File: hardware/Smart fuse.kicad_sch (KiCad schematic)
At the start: 2 parts, among them U14 SMART FUSE

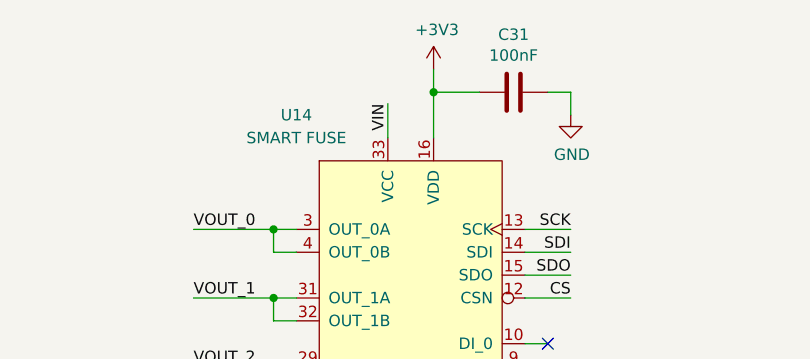
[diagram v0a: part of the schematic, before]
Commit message: changed clock and 5v converter coils, footprints rearrange commponets to fit the need now the board connector is vertical not horizontal relative to the pcb's longest side
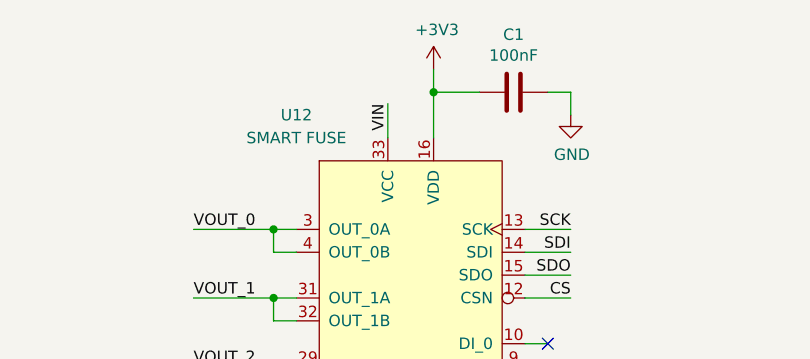
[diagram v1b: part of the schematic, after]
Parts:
- renumbered C31 to C1, U14 to U12
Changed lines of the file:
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@@
   (symbol (lib_id "power:GND") (at 144.78 137.16 0)
     (in_bom yes) (on_board yes)
-    (property "Reference" "#PWR069" (id 0) (at 144.78 143.51 0)
+    (property "Reference" "#PWR063" (id 0) (at 144.78 143.51 0)
       (effects (font (size 1.27 1.27)) hide)
     )
@@
   (symbol (lib_id "Device:C") (at 156.21 68.58 270)
     (in_bom yes) (on_board yes)
-    (property "Reference" "C31" (id 0) (at 156.21 62.1792 90))
+    (property "Reference" "C1" (id 0) (at 156.21 62.1792 90))
     (property "Value" "100nF" (id 1) (at 156.21 64.4906 90))
     (property "Footprint" "Capacitor_SMD:C_0603_1608Metric" (id 2) (at 152.4 69.5452 0)
@@
   (symbol (lib_id "power:GND") (at 162.56 71.12 0)
     (in_bom yes) (on_board yes)
-    (property "Reference" "#PWR071" (id 0) (at 162.56 77.47 0)
+    (property "Reference" "#PWR065" (id 0) (at 162.56 77.47 0)
       (effects (font (size 1.27 1.27)) hide)
     )
@@
   (symbol (lib_id "VN9D30Q100F:VN9D30Q100F") (at 144.78 76.2 0)
     (in_bom yes) (on_board yes)
-    (property "Reference" "U14" (id 0) (at 132.08 71.12 0))
+    (property "Reference" "U12" (id 0) (at 132.08 71.12 0))
     (property "Value" "SMART FUSE" (id 1) (at 132.08 73.66 0))
     (property "Footprint" "VN9D30Q100F:QFN-32_EP_6x6_Pitch0.5mm" (id 2) (at 154.94 72.39 0)
@@
   (symbol (lib_id "power:+3V3") (at 147.32 66.04 0)
     (in_bom yes) (on_board yes)
-    (property "Reference" "#PWR070" (id 0) (at 147.32 69.85 0)
+    (property "Reference" "#PWR064" (id 0) (at 147.32 69.85 0)
       (effects (font (size 1.27 1.27)) hide)
     )

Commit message: minor improvements
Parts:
- renumbered C1 to C32, U12 to U15
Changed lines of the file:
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@@
   (symbol (lib_id "power:GND") (at 144.78 137.16 0)
     (in_bom yes) (on_board yes)
-    (property "Reference" "#PWR063" (id 0) (at 144.78 143.51 0)
+    (property "Reference" "#PWR072" (id 0) (at 144.78 143.51 0)
       (effects (font (size 1.27 1.27)) hide)
     )
@@
   (symbol (lib_id "Device:C") (at 156.21 68.58 270)
     (in_bom yes) (on_board yes)
-    (property "Reference" "C1" (id 0) (at 156.21 62.1792 90))
+    (property "Reference" "C32" (id 0) (at 156.21 62.1792 90))
     (property "Value" "100nF" (id 1) (at 156.21 64.4906 90))
     (property "Footprint" "Capacitor_SMD:C_0603_1608Metric" (id 2) (at 152.4 69.5452 0)
@@
   (symbol (lib_id "power:GND") (at 162.56 71.12 0)
     (in_bom yes) (on_board yes)
-    (property "Reference" "#PWR065" (id 0) (at 162.56 77.47 0)
+    (property "Reference" "#PWR074" (id 0) (at 162.56 77.47 0)
       (effects (font (size 1.27 1.27)) hide)
     )
@@
   (symbol (lib_id "VN9D30Q100F:VN9D30Q100F") (at 144.78 76.2 0)
     (in_bom yes) (on_board yes)
-    (property "Reference" "U12" (id 0) (at 132.08 71.12 0))
+    (property "Reference" "U15" (id 0) (at 132.08 71.12 0))
     (property "Value" "SMART FUSE" (id 1) (at 132.08 73.66 0))
     (property "Footprint" "VN9D30Q100F:QFN-32_EP_6x6_Pitch0.5mm" (id 2) (at 154.94 72.39 0)
@@
   (symbol (lib_id "power:+3V3") (at 147.32 66.04 0)
     (in_bom yes) (on_board yes)
-    (property "Reference" "#PWR064" (id 0) (at 147.32 69.85 0)
+    (property "Reference" "#PWR073" (id 0) (at 147.32 69.85 0)
       (effects (font (size 1.27 1.27)) hide)
     )

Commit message: preproduction bug fixes
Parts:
- renumbered C32 to C1, U15 to U12
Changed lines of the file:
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@@
   (symbol (lib_id "power:GND") (at 144.78 137.16 0)
     (in_bom yes) (on_board yes)
-    (property "Reference" "#PWR072" (id 0) (at 144.78 143.51 0)
+    (property "Reference" "#PWR063" (id 0) (at 144.78 143.51 0)
       (effects (font (size 1.27 1.27)) hide)
     )
@@
   (symbol (lib_id "Device:C") (at 156.21 68.58 270)
     (in_bom yes) (on_board yes)
-    (property "Reference" "C32" (id 0) (at 156.21 62.1792 90))
+    (property "Reference" "C1" (id 0) (at 156.21 62.1792 90))
     (property "Value" "100nF" (id 1) (at 156.21 64.4906 90))
     (property "Footprint" "Capacitor_SMD:C_0603_1608Metric" (id 2) (at 152.4 69.5452 0)
@@
   (symbol (lib_id "power:GND") (at 162.56 71.12 0)
     (in_bom yes) (on_board yes)
-    (property "Reference" "#PWR074" (id 0) (at 162.56 77.47 0)
+    (property "Reference" "#PWR065" (id 0) (at 162.56 77.47 0)
       (effects (font (size 1.27 1.27)) hide)
     )
@@
   (symbol (lib_id "VN9D30Q100F:VN9D30Q100F") (at 144.78 76.2 0)
     (in_bom yes) (on_board yes)
-    (property "Reference" "U15" (id 0) (at 132.08 71.12 0))
+    (property "Reference" "U12" (id 0) (at 132.08 71.12 0))
     (property "Value" "SMART FUSE" (id 1) (at 132.08 73.66 0))
     (property "Footprint" "VN9D30Q100F:QFN-32_EP_6x6_Pitch0.5mm" (id 2) (at 154.94 72.39 0)
@@
   (symbol (lib_id "power:+3V3") (at 147.32 66.04 0)
     (in_bom yes) (on_board yes)
-    (property "Reference" "#PWR073" (id 0) (at 147.32 69.85 0)
+    (property "Reference" "#PWR064" (id 0) (at 147.32 69.85 0)
       (effects (font (size 1.27 1.27)) hide)
     )

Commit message: fuck
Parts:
- renumbered C1 to C31, U12 to U14
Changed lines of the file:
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@@
   (symbol (lib_id "power:GND") (at 144.78 137.16 0)
     (in_bom yes) (on_board yes)
-    (property "Reference" "#PWR063" (id 0) (at 144.78 143.51 0)
+    (property "Reference" "#PWR072" (id 0) (at 144.78 143.51 0)
       (effects (font (size 1.27 1.27)) hide)
     )
@@
   (symbol (lib_id "Device:C") (at 156.21 68.58 270)
     (in_bom yes) (on_board yes)
-    (property "Reference" "C1" (id 0) (at 156.21 62.1792 90))
+    (property "Reference" "C31" (id 0) (at 156.21 62.1792 90))
     (property "Value" "100nF" (id 1) (at 156.21 64.4906 90))
     (property "Footprint" "Capacitor_SMD:C_0603_1608Metric" (id 2) (at 152.4 69.5452 0)
@@
   (symbol (lib_id "power:GND") (at 162.56 71.12 0)
     (in_bom yes) (on_board yes)
-    (property "Reference" "#PWR065" (id 0) (at 162.56 77.47 0)
+    (property "Reference" "#PWR074" (id 0) (at 162.56 77.47 0)
       (effects (font (size 1.27 1.27)) hide)
     )
@@
   (symbol (lib_id "VN9D30Q100F:VN9D30Q100F") (at 144.78 76.2 0)
     (in_bom yes) (on_board yes)
-    (property "Reference" "U12" (id 0) (at 132.08 71.12 0))
+    (property "Reference" "U14" (id 0) (at 132.08 71.12 0))
     (property "Value" "SMART FUSE" (id 1) (at 132.08 73.66 0))
     (property "Footprint" "VN9D30Q100F:QFN-32_EP_6x6_Pitch0.5mm" (id 2) (at 154.94 72.39 0)
@@
   (symbol (lib_id "power:+3V3") (at 147.32 66.04 0)
     (in_bom yes) (on_board yes)
-    (property "Reference" "#PWR064" (id 0) (at 147.32 69.85 0)
+    (property "Reference" "#PWR073" (id 0) (at 147.32 69.85 0)
       (effects (font (size 1.27 1.27)) hide)
     )

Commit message: changed some footprints for clarity, and made some progress on board
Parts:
- renumbered C31 to C32, U14 to U15
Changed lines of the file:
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@@
   (symbol (lib_id "power:GND") (at 144.78 137.16 0)
     (in_bom yes) (on_board yes)
-    (property "Reference" "#PWR069" (id 0) (at 144.78 143.51 0)
+    (property "Reference" "#PWR072" (id 0) (at 144.78 143.51 0)
       (effects (font (size 1.27 1.27)) hide)
     )
@@
   (symbol (lib_id "Device:C") (at 156.21 68.58 270)
     (in_bom yes) (on_board yes)
-    (property "Reference" "C31" (id 0) (at 156.21 62.1792 90))
+    (property "Reference" "C32" (id 0) (at 156.21 62.1792 90))
     (property "Value" "100nF" (id 1) (at 156.21 64.4906 90))
     (property "Footprint" "Capacitor_SMD:C_0603_1608Metric" (id 2) (at 152.4 69.5452 0)
@@
   (symbol (lib_id "power:GND") (at 162.56 71.12 0)
     (in_bom yes) (on_board yes)
-    (property "Reference" "#PWR071" (id 0) (at 162.56 77.47 0)
+    (property "Reference" "#PWR074" (id 0) (at 162.56 77.47 0)
       (effects (font (size 1.27 1.27)) hide)
     )
@@
   (symbol (lib_id "VN9D30Q100F:VN9D30Q100F") (at 144.78 76.2 0)
     (in_bom yes) (on_board yes)
-    (property "Reference" "U14" (id 0) (at 132.08 71.12 0))
+    (property "Reference" "U15" (id 0) (at 132.08 71.12 0))
     (property "Value" "SMART FUSE" (id 1) (at 132.08 73.66 0))
     (property "Footprint" "VN9D30Q100F:QFN-32_EP_6x6_Pitch0.5mm" (id 2) (at 154.94 72.39 0)
@@
   (symbol (lib_id "power:+3V3") (at 147.32 66.04 0)
     (in_bom yes) (on_board yes)
-    (property "Reference" "#PWR070" (id 0) (at 147.32 69.85 0)
+    (property "Reference" "#PWR073" (id 0) (at 147.32 69.85 0)
       (effects (font (size 1.27 1.27)) hide)
     )

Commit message: finished new wersion of the board
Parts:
- renumbered C32 to C1, U15 to U12
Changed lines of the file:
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@@
   (symbol (lib_id "Device:C") (at 156.21 68.58 270)
     (in_bom yes) (on_board yes)
-    (property "Reference" "C32" (id 0) (at 156.21 62.1792 90))
+    (property "Reference" "C1" (id 0) (at 156.21 62.1792 90))
     (property "Value" "100nF" (id 1) (at 156.21 64.4906 90))
     (property "Footprint" "Capacitor_SMD:C_0603_1608Metric" (id 2) (at 152.4 69.5452 0)
@@
   (symbol (lib_id "VN9D30Q100F:VN9D30Q100F") (at 144.78 76.2 0)
     (in_bom yes) (on_board yes)
-    (property "Reference" "U15" (id 0) (at 132.08 71.12 0))
+    (property "Reference" "U12" (id 0) (at 132.08 71.12 0))
     (property "Value" "SMART FUSE" (id 1) (at 132.08 73.66 0))
     (property "Footprint" "VN9D30Q100F:QFN-32_EP_6x6_Pitch0.5mm" (id 2) (at 154.94 72.39 0)
